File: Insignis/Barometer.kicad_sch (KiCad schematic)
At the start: 3 parts, among them IC5 MS560702BA03-50

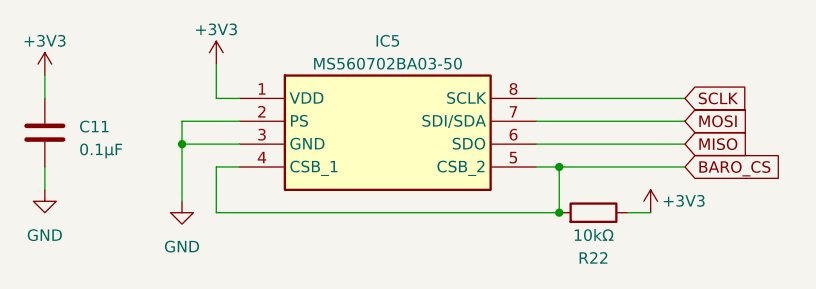
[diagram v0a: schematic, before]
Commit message: Fixed ERC errors
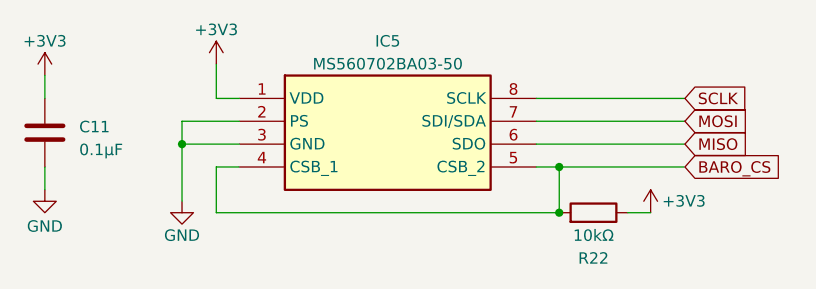
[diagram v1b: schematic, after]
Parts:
- IC5: footprint MS5607-02BA03 -> MS560702BA03-50:MS5607-02BA03
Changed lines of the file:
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@@
 			)
 		)
-		(property "Description" ""
+		(property "Description" "Power symbol creates a global label with name \"+3V3\""
 			(at 127 91.44 0)
 			(effects
@@
 					(size 1.27 1.27)
 				)
+				(hide yes)
 			)
 		)
@@
 			)
 		)
-		(property "Description" ""
+		(property "Description" "Power symbol creates a global label with name \"+3V3\""
 			(at 175.26 107.95 0)
 			(effects
@@
 					(size 1.27 1.27)
 				)
+				(hide yes)
 			)
 		)
@@
 		(on_board yes)
 		(dnp no)
-		(fields_autoplaced yes)
 		(property "Reference" "#PWR042"
 			(at 123.19 113.03 0)
@@
 		)
 		(property "Value" "GND"
-			(at 123.19 111.76 0)
+			(at 123.19 110.49 0)
 			(effects
 				(font
@@
 			)
 		)
-		(property "Description" ""
+		(property "Description" "Power symbol creates a global label with name \"GND\" , ground"
 			(at 123.19 106.68 0)
 			(effects
@@
 					(size 1.27 1.27)
 				)
+				(hide yes)
 			)
 		)
@@
 			)
 		)
-		(property "Footprint" "MS5607-02BA03"
+		(property "Footprint" "MS560702BA03-50:MS5607-02BA03"
 			(at 158.75 190.17 0)
 			(effects
@@
 			)
 		)
-		(property "Description" ""
+		(property "Description" "Power symbol creates a global label with name \"+3V3\""
 			(at 107.95 92.71 0)
 			(effects
@@
 					(size 1.27 1.27)
 				)
+				(hide yes)
 			)
 		)
@@
 		(on_board yes)
 		(dnp no)
-		(fields_autoplaced yes)
 		(property "Reference" "#PWR028"
 			(at 107.95 111.76 0)
@@
 		)
 		(property "Value" "GND"
-			(at 107.95 110.49 0)
+			(at 107.95 109.474 0)
 			(effects
 				(font
@@
 			)
 		)
-		(property "Description" ""
+		(property "Description" "Power symbol creates a global label with name \"GND\" , ground"
 			(at 107.95 105.41 0)
 			(effects
@@
 					(size 1.27 1.27)
 				)
-			)
-		)
+				(hide yes)
+			)
+		)
